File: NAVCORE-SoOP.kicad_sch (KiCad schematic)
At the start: 148 parts, among them J1 USB-C, J2 ESC 8P, J3 GPS+I2C, J8 microSD, P41 TEL_5V, P42 TEL_TX, P43 TEL_RX, P44 TEL_PPS, P45 TEL_RTS, P46 TEL_GND, P51 RC_5V, P52 RC_TX, P53 RC_RX, P54 RC_GND, P61 CAN_5V, P62 CANH, P63 CANL, P64 CAN_GND, P71 RF_5V, P72 RF_TX, P73 RF_RX, P74 RF_GND, Q1 AO3400A, Q3 AO3400A, SW1 BOOT, SW2 RESET, U1 STM32H743VIT6, U10 TLV75533, U11 SN65HVD230, U12 USBLC6-2SC6, U17 74LVC1G17, U18 TPS54202, U2 ICM-42688-P, U3 ICM-42605, U4 MS5611, U5 W25Q128JVSIQ, U6 PMW3901, U7 VL53L1X, U8 TPS54202, U9 AP2112K-3.3, Y1 8MHz

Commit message: rev B re-layout and re-route
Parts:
- removed C37, C38, C39: 100n, Capacitor_SMD:C_0402_1005Metric, symbol Device:C
- removed C40: 4u7, Capacitor_SMD:C_0805_2012Metric, symbol Device:C
- removed P42: TEL_TX, TestPoint:TestPoint_Pad_1.5x1.5mm, symbol Connector:TestPoint
- removed P43: TEL_RX, TestPoint:TestPoint_Pad_1.5x1.5mm, symbol Connector:TestPoint
- removed P45: TEL_RTS, TestPoint:TestPoint_Pad_1.5x1.5mm, symbol Connector:TestPoint
- removed P51: RC_5V, TestPoint:TestPoint_Pad_1.5x1.5mm, symbol Connector:TestPoint
- removed P52: RC_TX, TestPoint:TestPoint_Pad_1.5x1.5mm, symbol Connector:TestPoint
- removed P53: RC_RX, TestPoint:TestPoint_Pad_1.5x1.5mm, symbol Connector:TestPoint
- removed P54: RC_GND, TestPoint:TestPoint_Pad_1.5x1.5mm, symbol Connector:TestPoint
- removed R13: 10k, Resistor_SMD:R_0402_1005Metric, symbol Device:R
- removed U6: PMW3901, jlc:COB-28_L6.0-W6.0-P0.65-TL-EP, symbol jlc_parts:PMW3901MB-TXQT_C43496881
- removed U7: VL53L1X, jlc:OPTO-SMD_VL53L1CXV0FY-1, symbol jlc_parts:VL53L1CXV0FY/1
- added C49, C50, C59, C60, C61, C62, C63, C64: 100n, Capacitor_SMD:C_0402_1005Metric, symbol Device:C
- added C51: 1u, Capacitor_SMD:C_0402_1005Metric, symbol Device:C
- added C52: 100p, Capacitor_SMD:C_0402_1005Metric, symbol Device:C
- added C56, C57: 10n, Capacitor_SMD:C_0402_1005Metric, symbol Device:C
- added C58: 1n, Capacitor_SMD:C_0402_1005Metric, symbol Device:C
- added DZ1: BZT52C15, jlc:SOD-123_L2.7-W1.6-LS3.7-RD, symbol jlc_parts:BZT52C15
- added J11: SERIAL2 4P, jlc:CONN-SMD_4P-P1.00_SM04B-SRSS-TB-LF-SN, symbol jlc_parts:SM04B-SRSS-TB_(LF)(SN)
- added J12: U.FL ANT, Connector_Coaxial:U.FL_Hirose_U.FL-R-SMT-1_Vertical, symbol Connector:Conn_Coaxial
- added J5: RC IN, jlc:CONN-SMD_4P-P1.00_SM04B-SRSS-TB-LF-SN, symbol jlc_parts:SM04B-SRSS-TB_(LF)(SN)
- added J9: I2C 4P, jlc:CONN-SMD_4P-P1.00_SM04B-SRSS-TB-LF-SN, symbol jlc_parts:SM04B-SRSS-TB_(LF)(SN)
- added Q4: WST4041, jlc:SOT-23-3_L2.9-W1.3-P1.90-LS2.4-BR, symbol jlc_parts:WST4041
- added R28, R29: 0R, Resistor_SMD:R_0402_1005Metric, symbol Device:R
- added R30, R31: 10k, Resistor_SMD:R_0402_1005Metric, symbol Device:R
- added R34, R35: 1k, Resistor_SMD:R_0402_1005Metric, symbol Device:R
- added R36, R37: 4k7, Resistor_SMD:R_0402_1005Metric, symbol Device:R
- added R46: 100k, Resistor_SMD:R_0402_1005Metric, symbol Device:R
- added TP22: VSERVO, TestPoint:TestPoint_Pad_1.5x1.5mm, symbol Connector:TestPoint
- added U13: MAX2112, jlc:TQFN-28_L5.0-W5.0-P0.50-BL-EP3.3, symbol jlc_parts:MAX2112ETI+T
- added U14: OPA2374, jlc:SOP-8_L4.9-W3.9-P1.27-LS6.0-BL, symbol jlc_parts:OPA2374M/TR
- added Y2: 25MHz TCXO, jlc:OSC-SMD_4P-L3.2-W2.5-BL, symbol jlc_parts:YSOS510TP
- C17, C18: LCSC C70462 -> C16195875
- C68, C69, C70, C73, L5, PV1, Q3, R40, R41, R42, R43, R45, U18: now not fitted
- D1: LCSC C19077586 -> C19077573
- R6: LCSC LOOKUP:0402WGF3742TCE -> C25888
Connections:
- net +3V3A: now also C59.1, R28.1, U14.8 (VCC+), Y2.4 (VDD)
- net +5V: now also J11.1, J5.1, J9.1
- net GND: now also C49.2, C50.2, C51.2, C56.2, C57.2, C59.2, C60.2, C61.2, C62.2, C63.2, C64.2, J11.4, J11.5, J11.6, J12.2 (Ext), J5.4, J5.5, J5.6, J9.4, J9.5, J9.6, R29.1, R31.2, R35.1, R46.2, U13.10 (GNDTUNE), U13.11 (GNDSYN), U13.29 (EP), U13.3 (GND), U14.4 (VCC-), Y2.1 (GND), Y2.2 (GND)
- net I2C1_SCL: now also J9.2
- net I2C1_SDA: now also J9.3
- net I2C2_SCL: now also U13.27 (SCL)
- net I2C2_SDA: now also U13.26 (SDA)
- net RC_IN: now also J5.3
- net SOOP_I_ADC: now also U14.1 (OUT1)
- net SOOP_Q_ADC: now also U14.7 (OUT2)
- net SOOP_RSSI: now also R30.2
- net USART1_RX: now also J11.3
- net USART1_TX: now also J11.2
- net USART6_TX: now also J5.2
- net VBAT: now also DZ1.1 (K), Q4.2 (S); no longer D1.2 (A2), J2.2
- net EXT_CS1: no longer names the net of U1.85 (PD4)
- net TOF_INT: no longer names the net of U1.57 (PD10)
- net TOF_XSHUT: no longer names the net of U1.58 (PD11)
- net UART7_RTS: no longer names the net of U1.39 (PE9)
- net UART7_RX: no longer names the net of U1.37 (PE7)
- net UART7_TX: no longer names the net of U1.38 (PE8)
- new net ANT_IN: C52.1, J12.1 (In)
- new net CPOUT: R34.1, U13.12 (CPOUT)
- new net GC1: R35.2, U13.5 (GC1)
- new net IDC_N: C62.1, U13.22 (IDC-)
- new net IDC_P: C61.1, U13.21 (IDC+)
- new net IOUT_N: R37.1, U13.20 (IOUT-)
- new net IOUT_P: R36.1, U13.19 (IOUT+)
- new net LOOP: C57.1, R34.2
- new net OPA_IN1N: R37.2, U14.2 (IN1-)
- new net OPA_IN1P: R36.2, U14.3 (IN1+)
- new net QDC_N: C64.1, U13.24 (QDC-)
- new net QDC_P: C63.1, U13.23 (QDC+)
- new net QOUT_N: R31.1, U13.18 (QOUT-), U14.6 (IN2-)
- new net QOUT_P: R30.1, U13.17 (QOUT+), U14.5 (IN2+)
- new net RFIN: C52.2, U13.4 (RFIN)
- new net TUNER_ADDR: R29.2, U13.28 (ADDR)
- new net TUNER_REF: C58.1, Y2.3 (OUT)
- new net TUNER_XTAL: C58.2, U13.14 (XTAL)
- new net VBAT_GATE: DZ1.2 (A), Q4.1 (G), R46.1
- new net VBAT_IN: D1.2 (A2), J2.2, Q4.3 (D)
- new net VCC_RF: C49.1, C50.1, C51.1, R28.2, U13.1 (VCC_RF2), U13.13 (VCC_SYN), U13.16 (VCC_DIG), U13.2 (VCC_RF1), U13.25 (VCC_BB), U13.6 (VCC_LO), U13.7 (VCC_VCO)
- new net VCOBYP: C60.1, U13.8 (VCOBYP)
- new net VTUNE: C56.1, U13.9 (VTUNE)
- no-connect marks 60 -> 48

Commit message: re-route with freerouting and add the U19 temperature sensor
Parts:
- added C74: 100n, Capacitor_SMD:C_0402_1005Metric, symbol Device:C
- added U19: TMP119, jlc:DSBGA-6_L1.5-W1.0-R2-C3-P0.40-BL, symbol jlc_parts:TMP119AIYBGR
- U11: now not fitted
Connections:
- net +3V3: now also C74.1, U19.B1 (V+)
- net GND: now also C74.2, U19.B2 (GND), U19.C1 (ADD0)
- net I2C1_SCL: now also U19.A2 (SCL)
- net I2C1_SDA: now also U19.A1 (SDA)
- no-connect marks 48 -> 49

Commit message: Add the readiness gate, board ID 7180 and the runbook
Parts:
- removed C62, C64: 100n, Capacitor_SMD:C_0402_1005Metric, symbol Device:C
- removed R30: 10k, Resistor_SMD:R_0402_1005Metric, symbol Device:R
- removed TP11: SOOP_RSSI, TestPoint:TestPoint_Pad_1.5x1.5mm, symbol Connector:TestPoint
- removed Y2: 25MHz TCXO, jlc:OSC-SMD_4P-L3.2-W2.5-BL, symbol jlc_parts:YSOS510TP
- added C75: 1u, Capacitor_SMD:C_0402_1005Metric, symbol Device:C
- added C76, C77: 100p, Capacitor_SMD:C_0402_1005Metric, symbol Device:C
- added R47: 4k7, Resistor_SMD:R_0402_1005Metric, symbol Device:R
- added R48, R49, R50, R51, R52, R53: 10k, Resistor_SMD:R_0402_1005Metric, symbol Device:R
- added Y2: 25MHz TCXO, jlc:OSC-SMD_4P-L3.2-W2.5-BL, symbol jlc_parts:T132S4-25000ML33DTL
- C58: value 1n -> 10n; LCSC C1523 -> C15195
- C60, C61, C63: now fitted
- R31: value 10k -> 4k7; LCSC C25744 -> C25900
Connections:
- net +3V3A: now also R52.1, Y2.4 (VCC)
- net GND: now also U2.7 (RESV), U3.7 (RESV), C75.2, R53.2, Y2.1 (GND or N.C.), Y2.2 (GND); no longer C61.2, C63.2, R31.2
- net IDC_N: now also C61.2
- net OPA_IN1N: now also C76.1, R50.1
- net OPA_IN1P: now also R51.1
- net QDC_N: now also C63.2
- net QOUT_N: no longer U14.6 (IN2-)
- net QOUT_P: now also R47.1; no longer U14.5 (IN2+)
- net SOOP_I_ADC: now also C76.2, R50.2
- net SOOP_Q_ADC: now also C77.2, R48.2
- net TUNER_REF: now also Y2.3 (OUTPUT  RF)
- net SOOP_RSSI: no longer names the net of U1.33 (PC5)
- new net BB_VREF: C75.1, R49.2, R51.2, R52.2, R53.1
- new net OPA_IN2N: C77.1, R31.2, R48.1, U14.6 (IN2-)
- new net OPA_IN2P: R47.2, R49.1, U14.5 (IN2+)
- no-connect marks 49 -> 48

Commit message: SoOP solver end to end and SITL scenarios
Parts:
- removed U8: TPS54202, jlc:SOT-23-6_L2.9-W1.6-P0.95-LS2.8-BL, symbol jlc_parts:TPS54202DDCR
- added C78: 1u, Capacitor_SMD:C_0402_1005Metric, symbol Device:C
- added U8: LMR33630A, jlc:VQFN-12_L3.0-W2.0-P0.65-BL_TI_RNX, symbol jlc_parts:LMR33630ARNXR
- R6: value 37k4 -> 100k; LCSC C25888 -> C25741
- R7: value 5k1 -> 24k9; LCSC C25905 -> C25874
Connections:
- net BUCK_BOOT: now also U8.4 (BOOT)
- net BUCK_EN: now also U8.9 (EN)
- net BUCK_FB: now also U8.7 (FB)
- net BUCK_PH: now also U8.12 (SW), U8.3 (NC)
- net GND: now also C78.2, U8.1 (PGND), U8.11 (PGND), U8.6 (AGND)
- net VBAT: now also U8.10 (VIN), U8.2 (VIN)
- new net BUCK_VCC: C78.1, U8.5 (VCC)
- no-connect marks 48 -> 49

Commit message: Rev C: payload buck, CAN, pyro and touchdown; re-place and re-route
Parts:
- removed D1: SMBJ18A, jlc:DO-214AA_L4.4-W3.6-LS5.3-RD, symbol Device:D_TVS
- removed P61: CAN_5V, TestPoint:TestPoint_Pad_1.5x1.5mm, symbol Connector:TestPoint
- removed P62: CANH, TestPoint:TestPoint_Pad_1.5x1.5mm, symbol Connector:TestPoint
- removed P63: CANL, TestPoint:TestPoint_Pad_1.5x1.5mm, symbol Connector:TestPoint
- removed P64: CAN_GND, TestPoint:TestPoint_Pad_1.5x1.5mm, symbol Connector:TestPoint
- removed U18: TPS54202, jlc:SOT-23-6_L2.9-W1.6-P0.95-LS2.8-BL, symbol jlc_parts:TPS54202DDCR
- added C67, C79, C80: 1u, Capacitor_SMD:C_0402_1005Metric, symbol Device:C
- added D1: SMBJ26A, jlc:SMB_L4.6-W3.6-LS5.3-RD, symbol jlc_parts:SMBJ26A_C123820
- added D5: 1N4148W, jlc:SOD-123F_L2.7-W1.6-LS3.8-RD, symbol jlc_parts:1N4148W_C81598
- added D_USB: B5819W, jlc:SOD-123_L2.7-W1.6-LS3.7-RD-1, symbol jlc_parts:B5819W_C8598
- added F1: 3A, Fuse:Fuse_1206_3216Metric, symbol Device:Polyfuse_Small
- added J14: FLOW 6P, jlc:CONN-SMD_SH1.0MM-6P-WT, symbol jlc_parts:SH1_0MM-6P-WT
- added J15: LED 3P, jlc:CONN-SMD_3P-P1.00_SH1.0MM-3P-WT, symbol jlc_parts:SH1_0MM-3P-WT
- added J16: BUZZ 2P, jlc:CONN-SMD_2P-P1.00_SM02B-SRSS-TB-LF-SN, symbol jlc_parts:SM02B-SRSS-TB_(LF)(SN)
- added J17: SERVO 6P, jlc:CONN-SMD_SH1.0MM-6P-WT, symbol jlc_parts:SH1_0MM-6P-WT
- added J18: PYRO 2P, jlc:CONN-SMD_2P-P1.00_SM02B-SRSS-TB-LF-SN, symbol jlc_parts:SM02B-SRSS-TB_(LF)(SN)
- added J19: SWD 4P, jlc:CONN-SMD_4P-P1.00_SM04B-SRSS-TB-LF-SN, symbol jlc_parts:SM04B-SRSS-TB_(LF)(SN)
- added J20: TOUCH 2P, jlc:CONN-SMD_2P-P1.00_SM02B-SRSS-TB-LF-SN, symbol jlc_parts:SM02B-SRSS-TB_(LF)(SN)
- added J6: CAN 4P, jlc:CONN-SMD_4P-P1.00_SM04B-SRSS-TB-LF-SN, symbol jlc_parts:SM04B-SRSS-TB_(LF)(SN)
- added Q5: AO3400A, jlc:SOT-23-3_L2.9-W1.3-P1.90-LS2.4-BR, symbol jlc_parts:AO3400A
- added R54: 1k, Resistor_SMD:R_0402_1005Metric, symbol Device:R
- added R55: 47k, Resistor_SMD:R_0402_1005Metric, symbol Device:R
- added R56: 10k, Resistor_SMD:R_0402_1005Metric, symbol Device:R
- added U20: LMR33630A, jlc:VQFN-12_L3.0-W2.0-P0.65-BL_TI_RNX, symbol jlc_parts:LMR33630ARNXR
- added U21: XC6206P332MR, jlc:SOT-23-3_L2.9-W1.6-P1.90-LS2.8-BR, symbol jlc_parts:XC6206P332MR
- C17, C18: LCSC C16195875 -> C13585
- C68, C69, C70, C73, Q3, R40, R41, R42, R45, U11: now fitted
- L5: footprint Inductor_SMD:L_1210_3225Metric -> Inductor_SMD:L_APV_ANR4030; now fitted
- PV1: value VTX_9V -> PAYLOAD_5V; now fitted
- PV2: value VTX_GND -> PAYLOAD_GND
- R18: footprint Resistor_SMD:R_0402_1005Metric -> Resistor_SMD:R_0603_1608Metric; LCSC C25744 -> C25804
- R43: value 6k8 -> 24k9; LCSC C25917 -> C25874; now fitted
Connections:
- net +3V3: now also J14.1, J19.1, R56.2; no longer C41.1, U11.3 (VCC)
- net +5V: now also D_USB.1 (-), J16.1; no longer J11.1, PL2.1
- net BUZZ_DRAIN: now also J16.2
- net CANH: now also J6.2
- net CANL: now also J6.3
- net GND: now also C67.2, C79.2, C80.2, D1.2 (A), J14.6, J14.7, J14.8, J15.3, J15.4, J15.5, J16.3, J16.4, J17.6, J17.7, J17.8, J18.3, J18.4, J19.4, J19.5, J19.6, J20.2, J20.3, J20.4, J6.4, J6.5, J6.6, Q5.2 (S), R55.2, U20.1 (PGND), U20.11 (PGND), U20.6 (AGND), U21.1 (GND)
- net SPI3_MISO: now also J14.3
- net SPI3_MOSI: now also J14.4
- net SPI3_SCK: now also J14.2
- net SWCLK: now also J19.3
- net SWDIO: now also J19.2
- net VBAT: now also F1.1, U20.10 (VIN), U20.2 (VIN)
- net VBAT_IN: now also D1.1 (C)
- net VBUS: now also D_USB.2 (+)
- net WS2812_OUT: now also J15.2
- net PYRO_FIRE: now reaches U1.33 (PC5)
- net PYRO_FIRE: now also R54.1
- net TOUCHDOWN: now reaches U1.57 (PD10)
- net TOUCHDOWN: now also J20.1, R56.1
- net PWM7: now reaches U1.59 (PD12)
- net PWM7: now also J17.1
- net PWM8: now reaches U1.60 (PD13)
- net PWM8: now also J17.2
- net PWM9: now reaches U1.61 (PD14)
- net PWM9: now also J17.3
- net PWM10: now reaches U1.62 (PD15)
- net PWM10: now also J17.4
- net EXT_CS1: now reaches U1.85 (PD4)
- net EXT_CS1: now also J14.5
- net +9V renamed +5V_PAYLOAD
- net +5V_PAYLOAD: now also J11.1, PL2.1, C80.1, J15.1, J17.5, J6.1, U21.3 (Vin)
- net BUCK9_BOOT renamed BUCK_PAYLOAD_BOOT
- net BUCK_PAYLOAD_BOOT: now also U20.4 (BOOT)
- net BUCK9_EN renamed BUCK_PAYLOAD_EN
- net BUCK_PAYLOAD_EN: now also U20.9 (EN)
- net BUCK9_FB renamed BUCK_PAYLOAD_FB
- net BUCK_PAYLOAD_FB: now also U20.7 (FB)
- net BUCK9_PH renamed BUCK_PAYLOAD_PH
- net BUCK_PAYLOAD_PH: now also U20.12 (SW), U20.3 (NC)
- net VTX_EN renamed PAYLOAD_EN
- new net +3V3_CAN: C67.1, U11.3 (VCC), U21.2 (Vout)
- new net BUCK_PAYLOAD_VCC: C79.1, U20.5 (VCC)
- new net PYRO_DRAIN: D5.2 (A), J18.2, Q5.3 (D)
- new net PYRO_GATE: Q5.1 (G), R54.2, R55.1
- new net VBAT_FUSED: D5.1 (K), F1.2, J18.1
- no-connect marks 49 -> 44

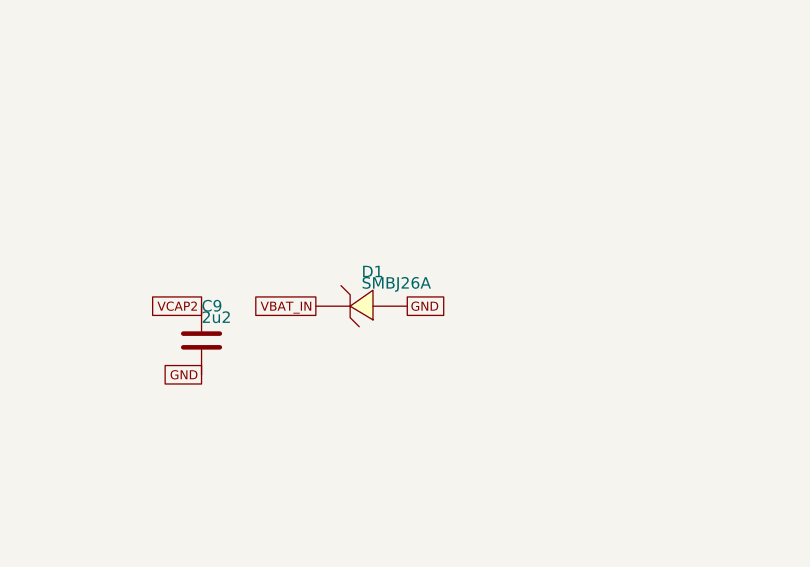
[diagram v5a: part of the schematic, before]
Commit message: Rev C: rate the input for 5S and budget the payload rail
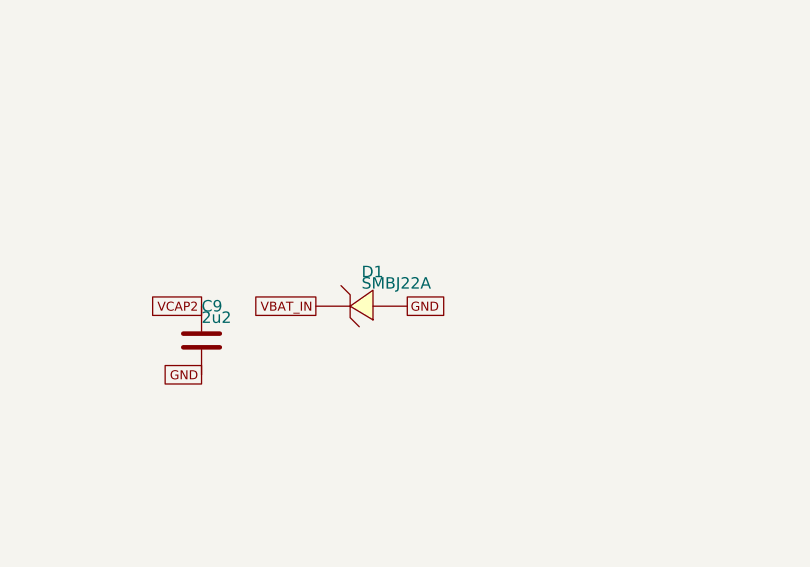
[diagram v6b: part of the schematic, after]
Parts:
- removed D1: SMBJ26A, jlc:SMB_L4.6-W3.6-LS5.3-RD, symbol jlc_parts:SMBJ26A_C123820
- added D1: SMBJ22A, jlc:SMB_L4.6-W3.6-LS5.3-RD, symbol jlc_parts:SMBJ22A_C113993
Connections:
- net GND: now also D1.2 (A)
- net VBAT_IN: now also D1.1 (C)
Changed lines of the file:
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@@
 		(effects (font (size 1.0 1.0)) (justify right))
 	)
-	(symbol (lib_id "jlc_parts:SMBJ26A_C123820") (at 577.85 295.91 0) (unit 0)
+	(symbol (lib_id "jlc_parts:SMBJ22A_C113993") (at 577.85 295.91 0) (unit 0)
 		(exclude_from_sim no) (in_bom yes) (on_board yes) (dnp no)
 		(property "Reference" "D1" (at 577.85 292.10 0) (effects (font (size 1.27 1.27)) (justify left)))
-		(property "Value" "SMBJ26A" (at 577.85 293.37 0) (effects (font (size 1.27 1.27)) (justify left)))
+		(property "Value" "SMBJ22A" (at 577.85 293.37 0) (effects (font (size 1.27 1.27)) (justify left)))
 		(property "Footprint" "jlc:SMB_L4.6-W3.6-LS5.3-RD" (at 577.85 295.91 0) (effects (font (size 1.27 1.27)) hide))
-		(property "LCSC" "C123820" (at 577.85 295.91 0) (effects (font (size 1.27 1.27)) hide))
+		(property "LCSC" "C113993" (at 577.85 295.91 0) (effects (font (size 1.27 1.27)) hide))
 		(pin "1")
 		(pin "2")

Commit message: clean up copper and silkscreen, align the CPL to JLC footprints, clear J14 off the USB-C
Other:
- company: (none) -> Krystian Filipek - University of Cambridge / CUSF
- title: (none) -> NAVCORE-SoOP flight controller
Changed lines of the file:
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@@
 	(generator_version "9.0")
 	(paper "User" 1100 850)
+	(title_block
+		(title "NAVCORE-SoOP flight controller")
+		(date "2026-09-23")
+		(rev "C")
+		(company "Krystian Filipek - University of Cambridge / CUSF")
+		(comment 1 "6-layer STM32H743 flight controller with Iridium SoOP Doppler navigation")
+		(comment 2 "Generated from tools/design.py by tools/gen_sch.py - edit the source, not this file")
+	)
 	(symbol (lib_id "jlc_parts:STM32H743VIT6_C114409") (at 26.67 109.22 0) (unit 0)
 		(exclude_from_sim no) (in_bom yes) (on_board yes) (dnp no)

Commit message: Fix the tuner loop filter and IMU chip select, mark the forward edge
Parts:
- added C81, C84, C86: 1n, Capacitor_SMD:C_0402_1005Metric, symbol Device:C
- added R57: 470R, Resistor_SMD:R_0402_1005Metric, symbol Device:R
- added R58: 4k7, Resistor_SMD:R_0402_1005Metric, symbol Device:R
- C56: value 10n -> 100p; LCSC C15195 -> C1546
- C57: value 10n -> 100n; LCSC C15195 -> C1525
- R34: value 1k -> 330R; LCSC C11702 -> C25104
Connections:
- net CPOUT: now also C81.1, R57.1
- net GC1: now also R58.2
- net GND: now also C81.2, C84.2, C86.2
- net VCC_RF: now also C84.1, C86.1, R58.1
- net VTUNE: now also R57.2
